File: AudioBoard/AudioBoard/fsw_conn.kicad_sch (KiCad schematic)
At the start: 0 parts

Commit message: added first time routing to see crosssections
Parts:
- added J10: Conn_02x05_Counter_Clockwise, symbol Connector_Generic:Conn_02x05_Counter_Clockwise
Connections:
- new net DVDD: J10.3 (Pin_3)
- new net GND: J10.4 (Pin_4)
- new net I2C.SCLK: J10.2 (Pin_2)
- new net I2C.SDO: J10.1 (Pin_1)

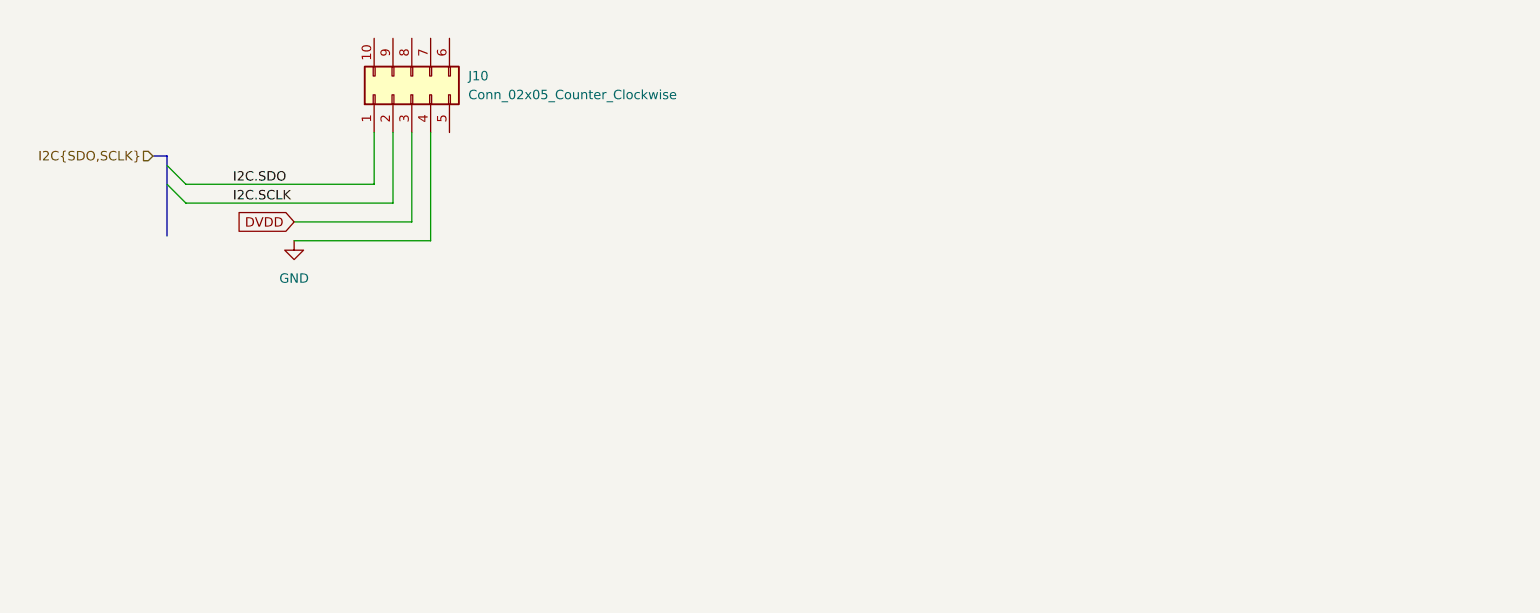
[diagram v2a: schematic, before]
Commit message: added bias voltage buffer, fixed fsw shift reg input filter
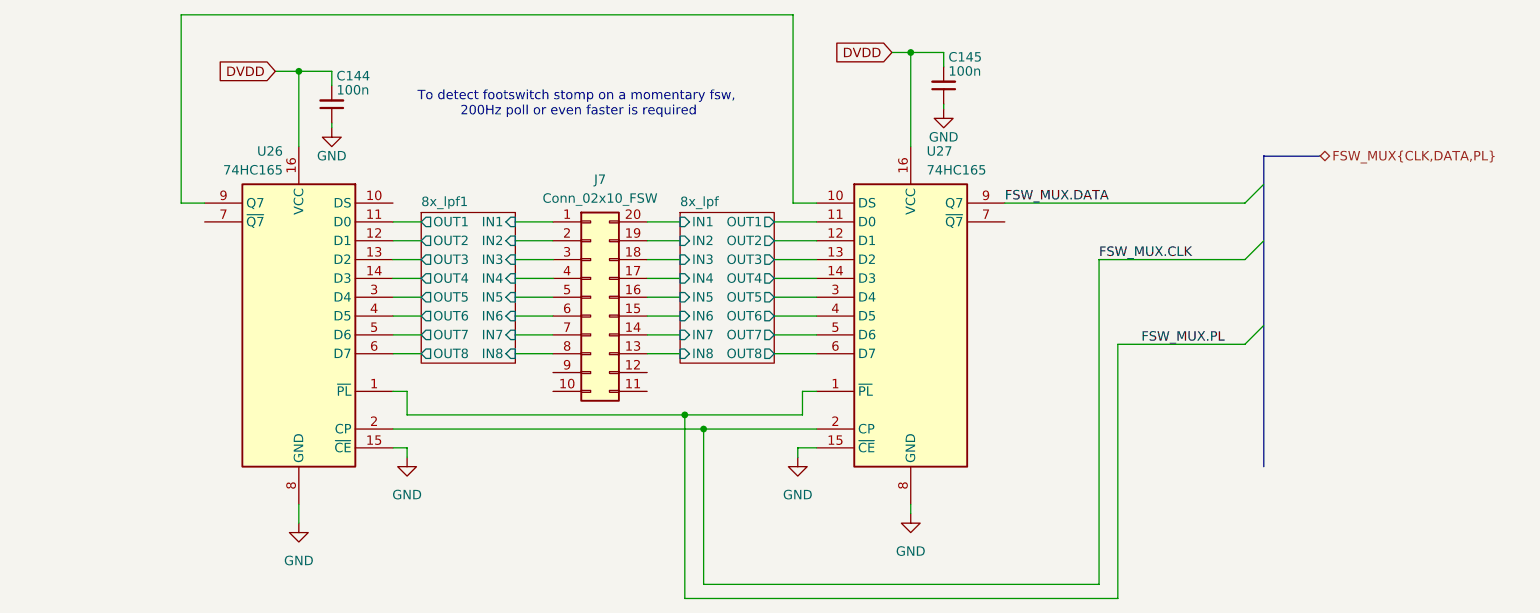
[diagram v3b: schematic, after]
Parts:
- removed J10: Conn_02x05_Counter_Clockwise, symbol Connector_Generic:Conn_02x05_Counter_Clockwise
- added C144, C145: 100n, Capacitor_SMD:C_0402_1005Metric, symbol Device:C_Small
- added J7: Conn_02x10_FSW, Connector_PinSocket_1.27mm:PinSocket_2x10_P1.27mm_Vertical, symbol Connector_Generic:Conn_02x10_Counter_Clockwise
- added U26, U27: 74HC165, Package_SO:SOIC-16_3.9x9.9mm_P1.27mm, symbol 74xx:74HC165
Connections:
- net DVDD: now also C144.2, C145.2, U26.16 (VCC), U27.16 (VCC)
- net GND: now also C144.1, C145.1, U26.15 (~{CE}), U26.8 (GND), U27.15 (~{CE}), U27.8 (GND)
- new net: U26.9 (Q7), U27.10 (DS)
- new net 8x_lpf/IN1: J7.20 (Pin_20)
- new net 8x_lpf/IN2: J7.19 (Pin_19)
- new net 8x_lpf/IN3: J7.18 (Pin_18)
- new net 8x_lpf/IN4: J7.17 (Pin_17)
- new net 8x_lpf/IN5: J7.16 (Pin_16)
- new net 8x_lpf/IN6: J7.15 (Pin_15)
- new net 8x_lpf/IN7: J7.14 (Pin_14)
- new net 8x_lpf/IN8: J7.13 (Pin_13)
- new net 8x_lpf/OUT1: U27.11 (D0)
- new net 8x_lpf/OUT2: U27.12 (D1)
- new net 8x_lpf/OUT3: U27.13 (D2)
- new net 8x_lpf/OUT4: U27.14 (D3)
- new net 8x_lpf/OUT5: U27.3 (D4)
- new net 8x_lpf/OUT6: U27.4 (D5)
- new net 8x_lpf/OUT7: U27.5 (D6)
- new net 8x_lpf/OUT8: U27.6 (D7)
- new net 8x_lpf1/IN1: J7.1 (Pin_1)
- new net 8x_lpf1/IN2: J7.2 (Pin_2)
- new net 8x_lpf1/IN3: J7.3 (Pin_3)
- new net 8x_lpf1/IN4: J7.4 (Pin_4)
- new net 8x_lpf1/IN5: J7.5 (Pin_5)
- new net 8x_lpf1/IN6: J7.6 (Pin_6)
- new net 8x_lpf1/IN7: J7.7 (Pin_7)
- new net 8x_lpf1/IN8: J7.8 (Pin_8)
- new net 8x_lpf1/OUT1: U26.11 (D0)
- new net 8x_lpf1/OUT2: U26.12 (D1)
- new net 8x_lpf1/OUT3: U26.13 (D2)
- new net 8x_lpf1/OUT4: U26.14 (D3)
- new net 8x_lpf1/OUT5: U26.3 (D4)
- new net 8x_lpf1/OUT6: U26.4 (D5)
- new net 8x_lpf1/OUT7: U26.5 (D6)
- new net 8x_lpf1/OUT8: U26.6 (D7)
- new net FSW_MUX.CLK: U26.2 (CP), U27.2 (CP)
- new net FSW_MUX.DATA: U27.9 (Q7)
- new net FSW_MUX.PL: U26.1 (~{PL}), U27.1 (~{PL})
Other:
- added sheet 8x_lpf (8x_lpf.kicad_sch)
- added sheet 8x_lpf1 (8x_lpf.kicad_sch)
- note added: "To detect footswitch stomp on a momentary fsw, 200Hz poll or even faster is required"
